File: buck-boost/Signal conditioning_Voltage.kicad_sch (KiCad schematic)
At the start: 16 parts, among them U11 Opamp_Dual, U13 Opamp_Dual

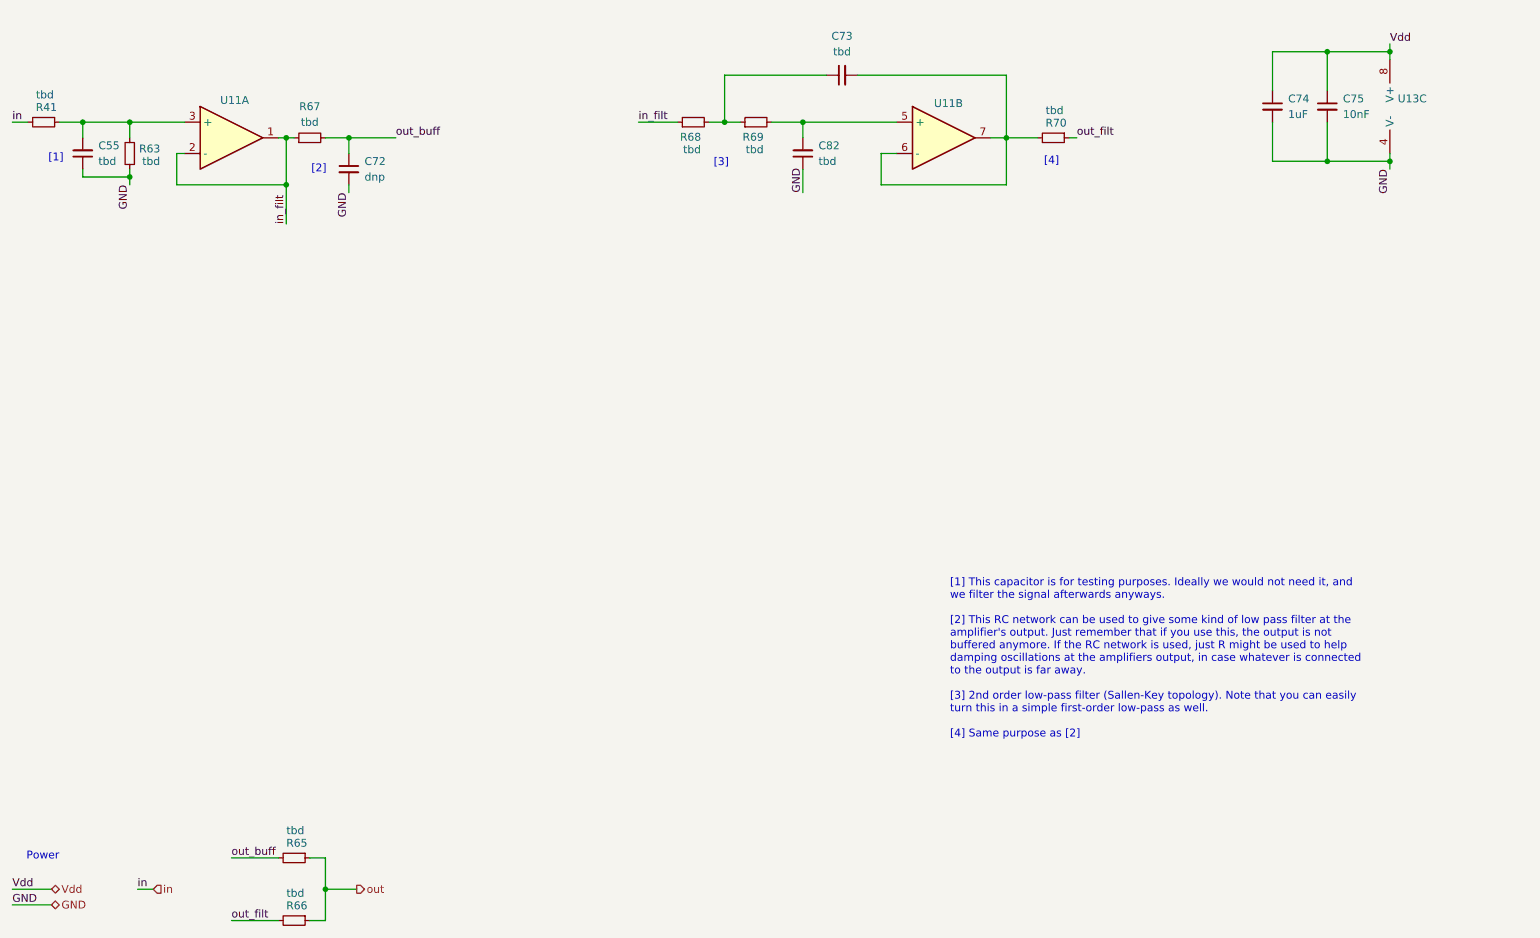
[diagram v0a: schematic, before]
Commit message: The changes indicated in the text document Review. 05.11.2024 were implemented. Missing footprints were added
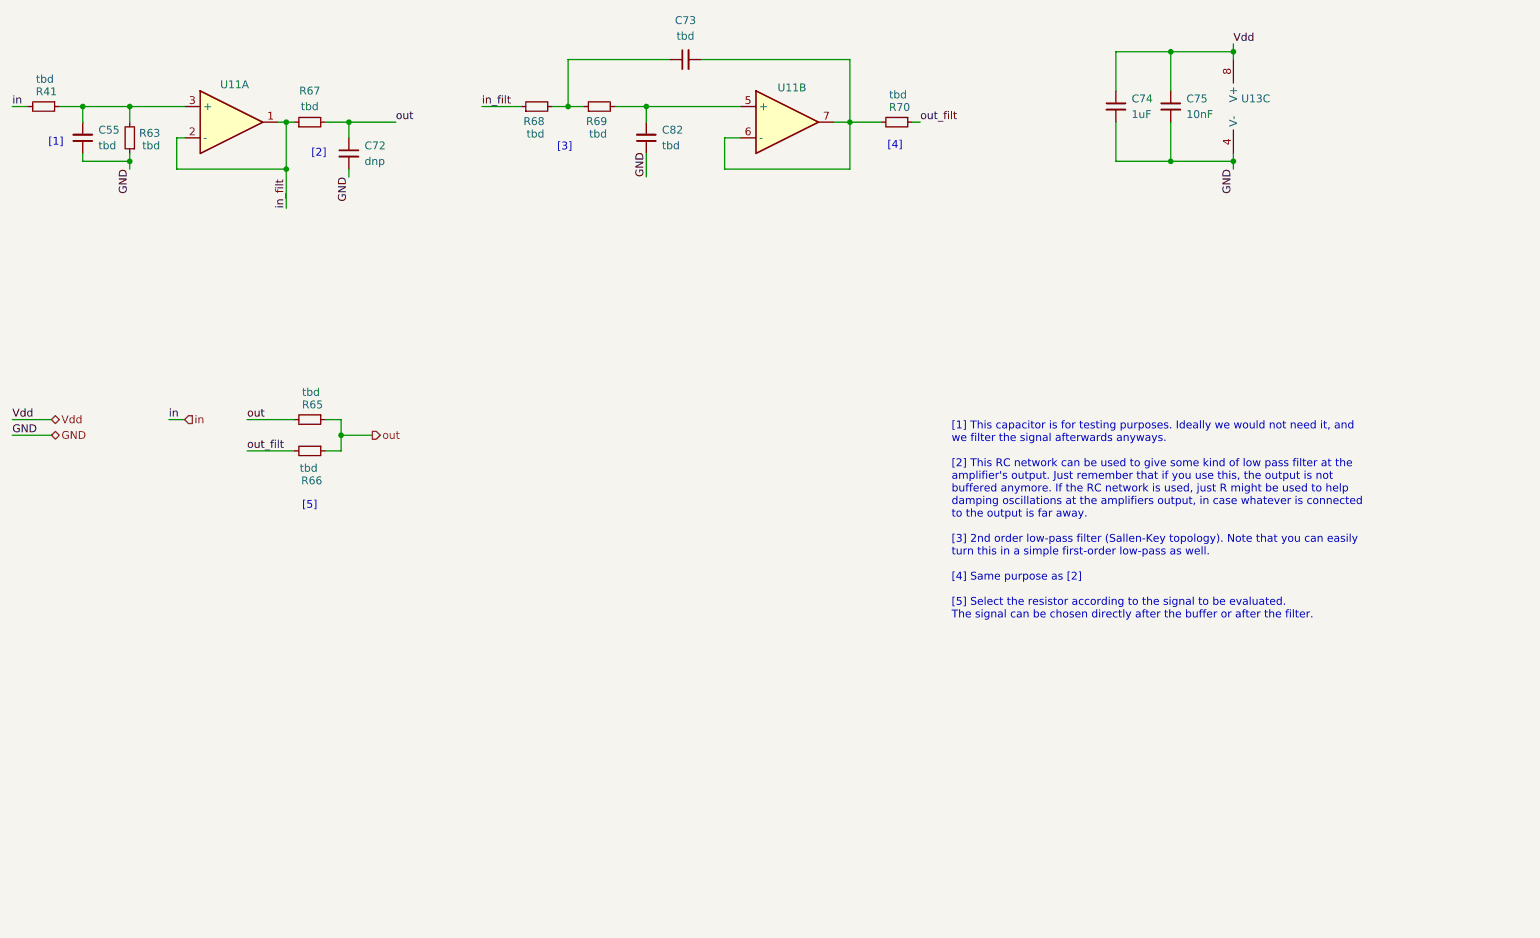
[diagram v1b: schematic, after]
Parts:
- U11, U13: footprint (none) -> Package_SO:SOIC-8_3.9x4.9mm_P1.27mm
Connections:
- net out_buff is gone; now on net out: C72.1, R65.2, R67.2
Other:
- note added: "[5]"
- note removed: "Power"
- moved on the sheet: C55, C72, C73, C74, C75, C82, R41, R63, R65, R66, R67, R68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

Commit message: Some errors in the schematics were corrected. PCB file V1.0
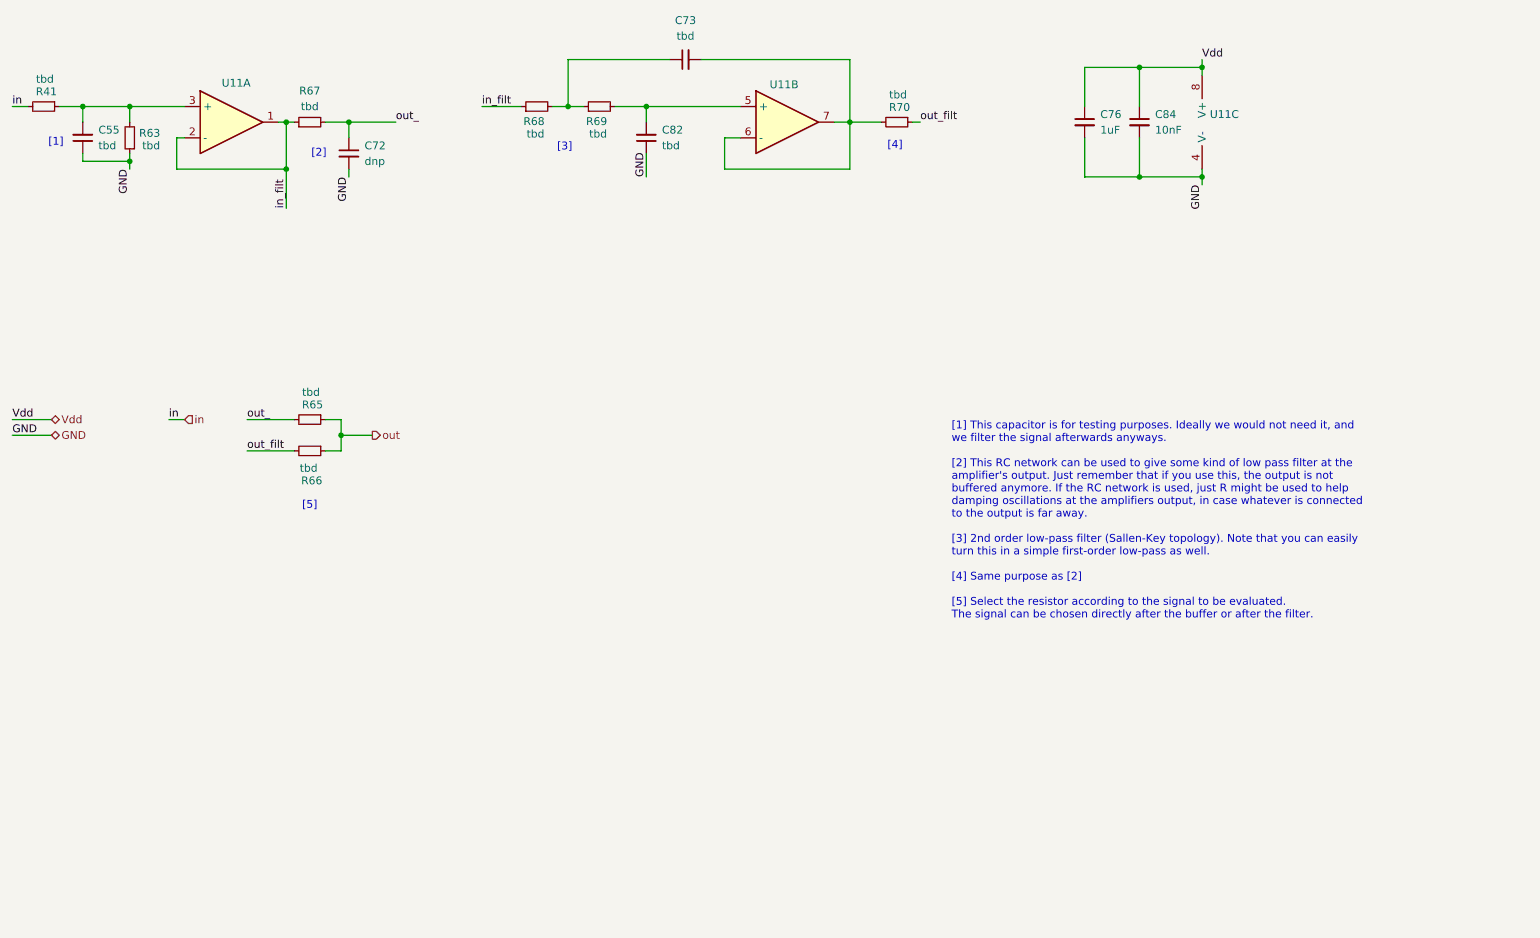
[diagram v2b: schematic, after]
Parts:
- removed C74: 1uF, Capacitor_SMD:C_0805_2012Metric_Pad1.18x1.45mm_HandSolder, symbol Device:C_Small
- removed C75: 10nF, Capacitor_SMD:C_0805_2012Metric_Pad1.18x1.45mm_HandSolder, symbol Device:C_Small
- removed U13: Opamp_Dual, Package_SO:SOIC-8_3.9x4.9mm_P1.27mm, symbol Device:Opamp_Dual
- added C76: 1uF, Capacitor_SMD:C_0805_2012Metric_Pad1.18x1.45mm_HandSolder, symbol Device:C_Small
- added C84: 10nF, Capacitor_SMD:C_0805_2012Metric_Pad1.18x1.45mm_HandSolder, symbol Device:C_Small
- added unit 3 of U11
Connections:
- net GND: now also C76.2, C84.2, U11.4 (V-)
- net Vdd: now also C76.1, C84.1, U11.8 (V+)
- net out: no longer C72.1, R65.2, R67.2
- new net out_: C72.1, R65.2, R67.2
